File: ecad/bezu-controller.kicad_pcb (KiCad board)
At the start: 2 copper layers, 84 parts, among them Q1 40N06D, Q10 40N06D, Q11 40N06D, Q12 40N06D, Q13 40N06D, Q14 40N06D, Q15 40N06D, Q16 40N06D, Q17 40N06D, Q18 40N06D, Q19 40N06D, Q2 40N06D, Q20 40N06D, Q21 40N06D, Q22 40N06D, Q23 40N06D, Q24 40N06D, Q3 40N06D, Q4 40N06D, Q5 40N06D, Q6 40N06D, Q7 40N06D, Q8 40N06D, Q9 40N06D, U1 LM2105D, U10 LM2105D, U11 LM2105D, U12 LM2105D, U2 LM2105D, U3 LM2105D, U4 LM2105D, U5 LM2105D, U6 LM2105D, U7 LM2105D, U8 LM2105D, U9 LM2105D

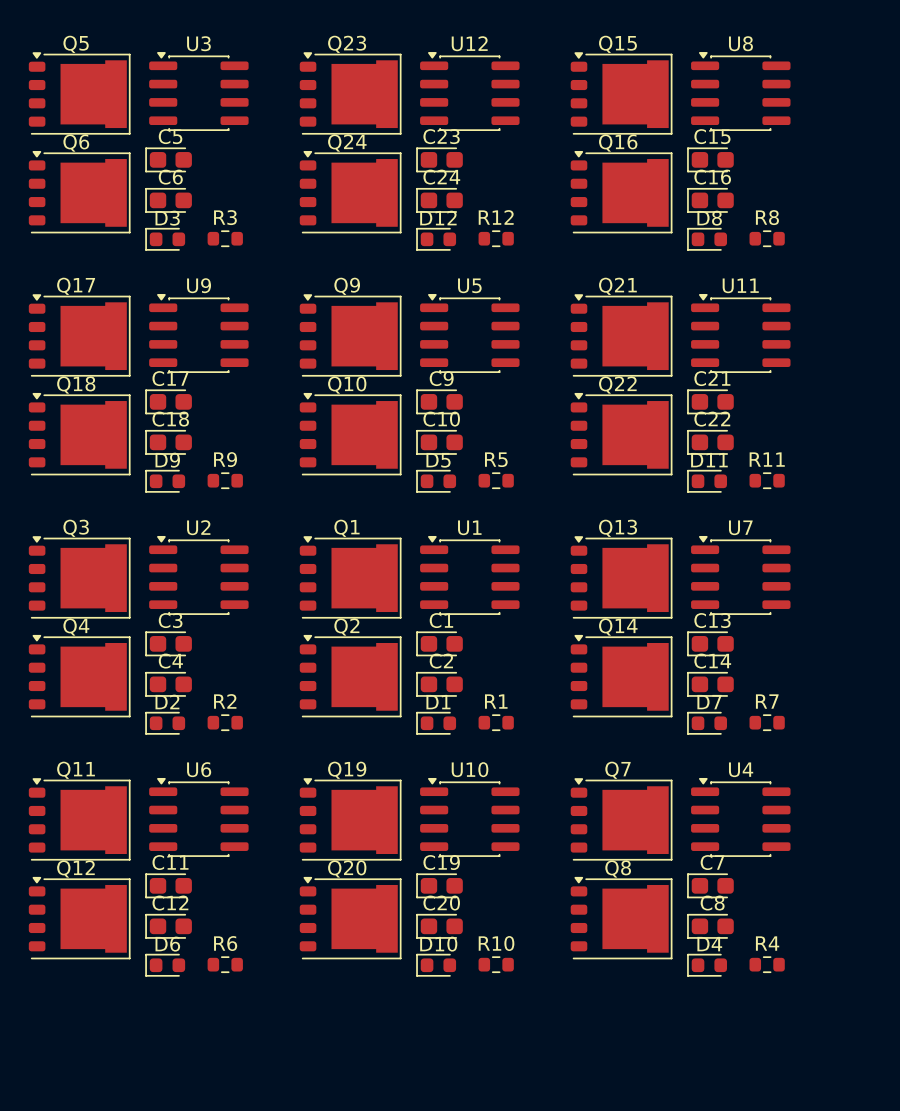
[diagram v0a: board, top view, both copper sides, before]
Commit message: Use IRS2104
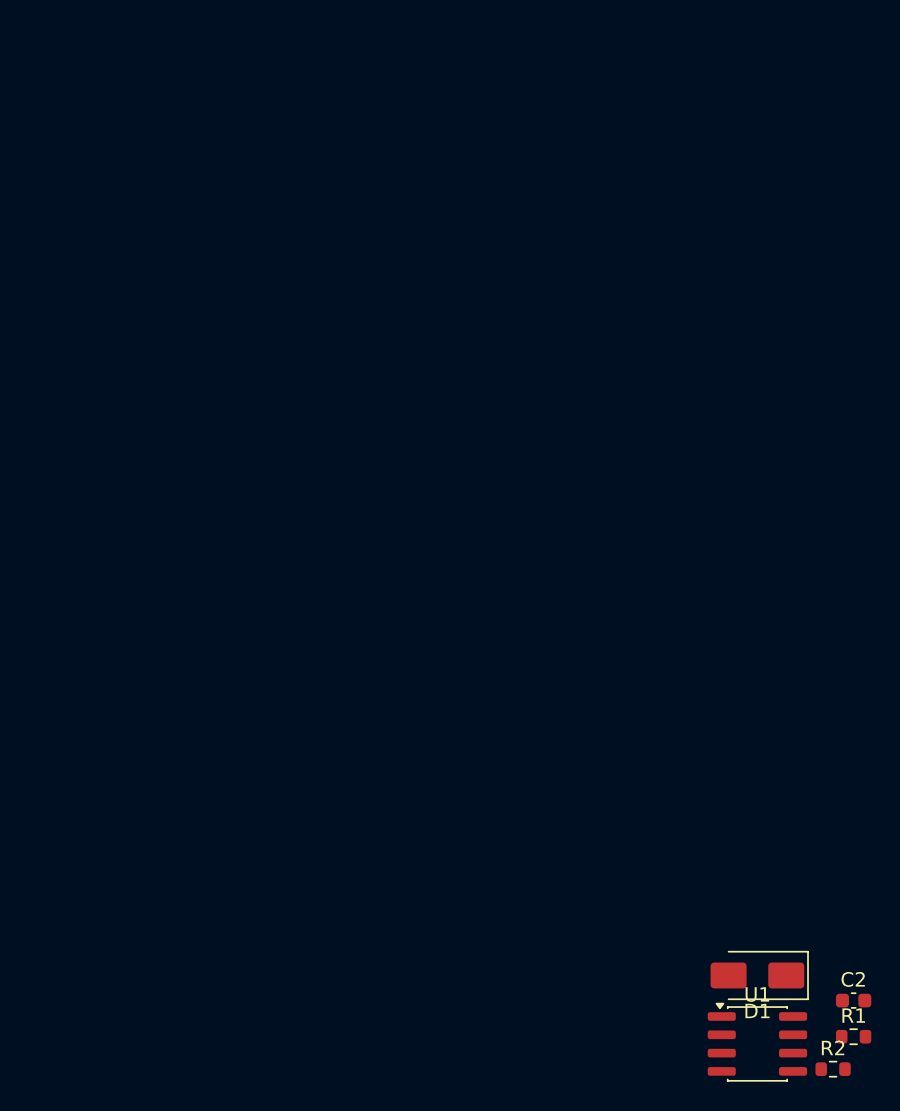
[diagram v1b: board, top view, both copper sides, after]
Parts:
- removed C1, C10, C11, C12, C13, C14, C15, C16, C17, C18, C19, C20, C21, C22, C23, C24, C3, C4, C5, C6, C7, C8, C9: C, Capacitor_Tantalum_SMD:CP_EIA-2012-12_Kemet-R
- removed D10, D11, D12, D2, D3, D4, D5, D6, D7, D8, D9: D, Diode_SMD:D_0603_1608Metric
- removed Q1, Q10, Q11, Q12, Q13, Q14, Q15, Q16, Q17, Q18, Q19, Q2, Q20, Q21, Q22, Q23, Q24, Q3, Q4, Q5, Q6, Q7, Q8, Q9: 40N06D, Package_DFN_QFN:PQFN-8-EP_6x5mm_P1.27mm_Generic
- removed R10, R11, R12, R3, R4, R5, R6, R7, R8, R9: R, Resistor_SMD:R_0603_1608Metric
- removed U10, U11, U12, U2, U3, U4, U5, U6, U7, U8, U9: LM2105D, Package_SO:SOIC-8_3.9x4.9mm_P1.27mm
- C2: footprint Capacitor_Tantalum_SMD:CP_EIA-2012-12_Kemet-R -> Capacitor_SMD:C_0603_1608Metric
- D1: value D -> ES1D; footprint Diode_SMD:D_0603_1608Metric -> Diode_SMD:D_SMA
- U1: value LM2105D -> IR2104
- moved R2 48.5 mm to (165.8, 123.2)
- moved U1 38.0 mm to (160.5, 121.5)
- moved C2 36.0 mm to (167.2, 118.5)
- moved R1 33.0 mm to (167.2, 121.0)
- moved D1 28.2 mm to (160.5, 116.8), turned to 180 degrees
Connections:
- C2 pad 1: unconnected-(C2-Pad1) -> Net-(D1-K)
- C2 pad 2: unconnected-(C2-Pad2) -> /H-Bridge/OUT
- D1 pad 1: (no net) -> Net-(D1-K)
- D1 pad 2: unconnected-(Q2-PadS) -> +12V
- R1 pad 1: unconnected-(Q2-PadS) -> Net-(U1-HO)
- R1 pad 2: (no net) -> Net-(Q1-PadG)
- R2 pad 1: Net-(D2-A) -> Net-(U1-LO)
- U1 pad 1: VDD -> +12V
- U1 pad 2: (no net) -> /H-Bridge/IN
- U1 pad 3: (no net) -> /H-Bridge/~{SD}
- U1 pad 5: (no net) -> Net-(U1-LO)
- U1 pad 6: unconnected-(C2-Pad2) -> /H-Bridge/OUT
- U1 pad 7: unconnected-(Q2-PadG) -> Net-(U1-HO)
- U1 pad 8: unconnected-(C2-Pad1) -> Net-(D1-K)

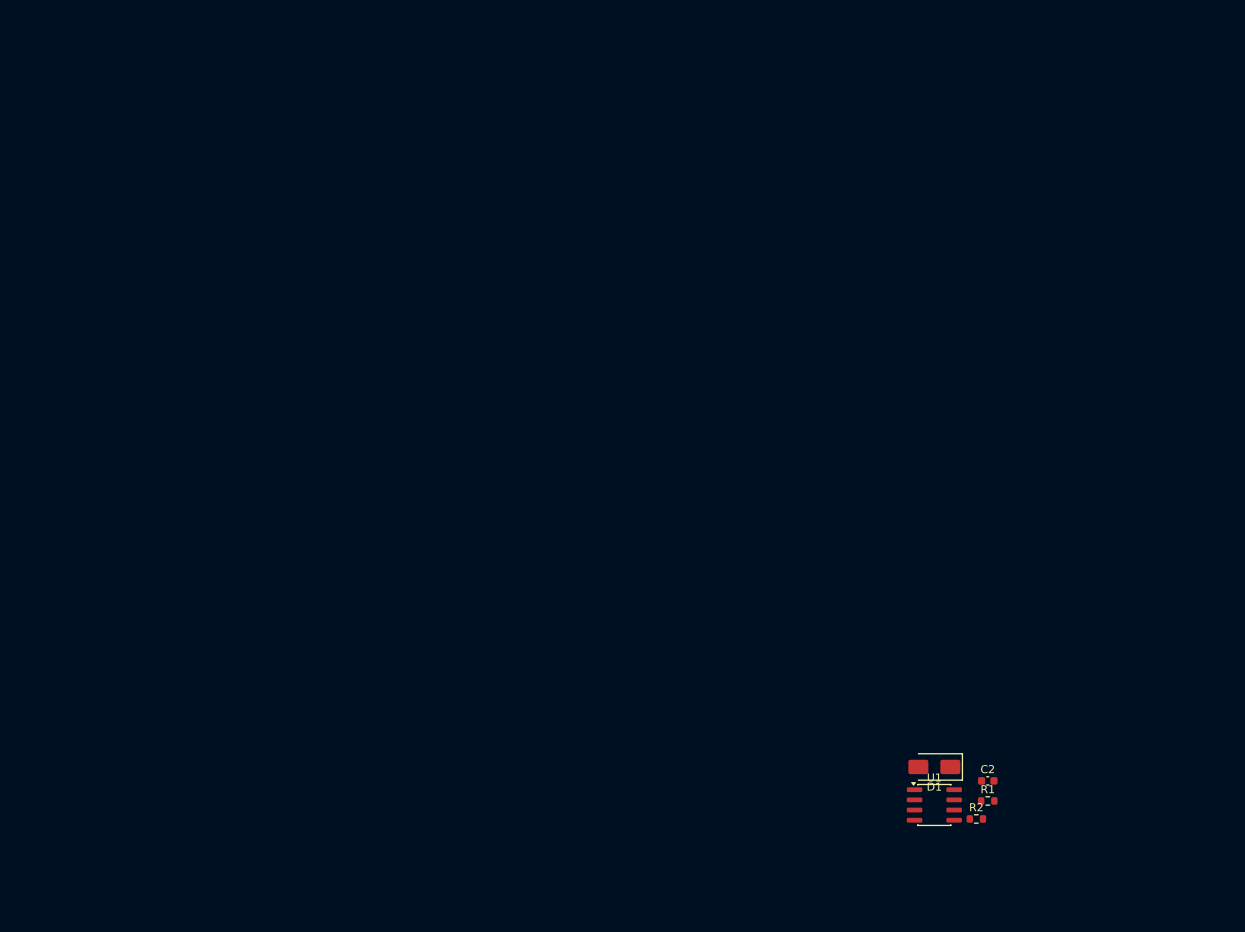
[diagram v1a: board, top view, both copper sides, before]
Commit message: Initial half bridge layout
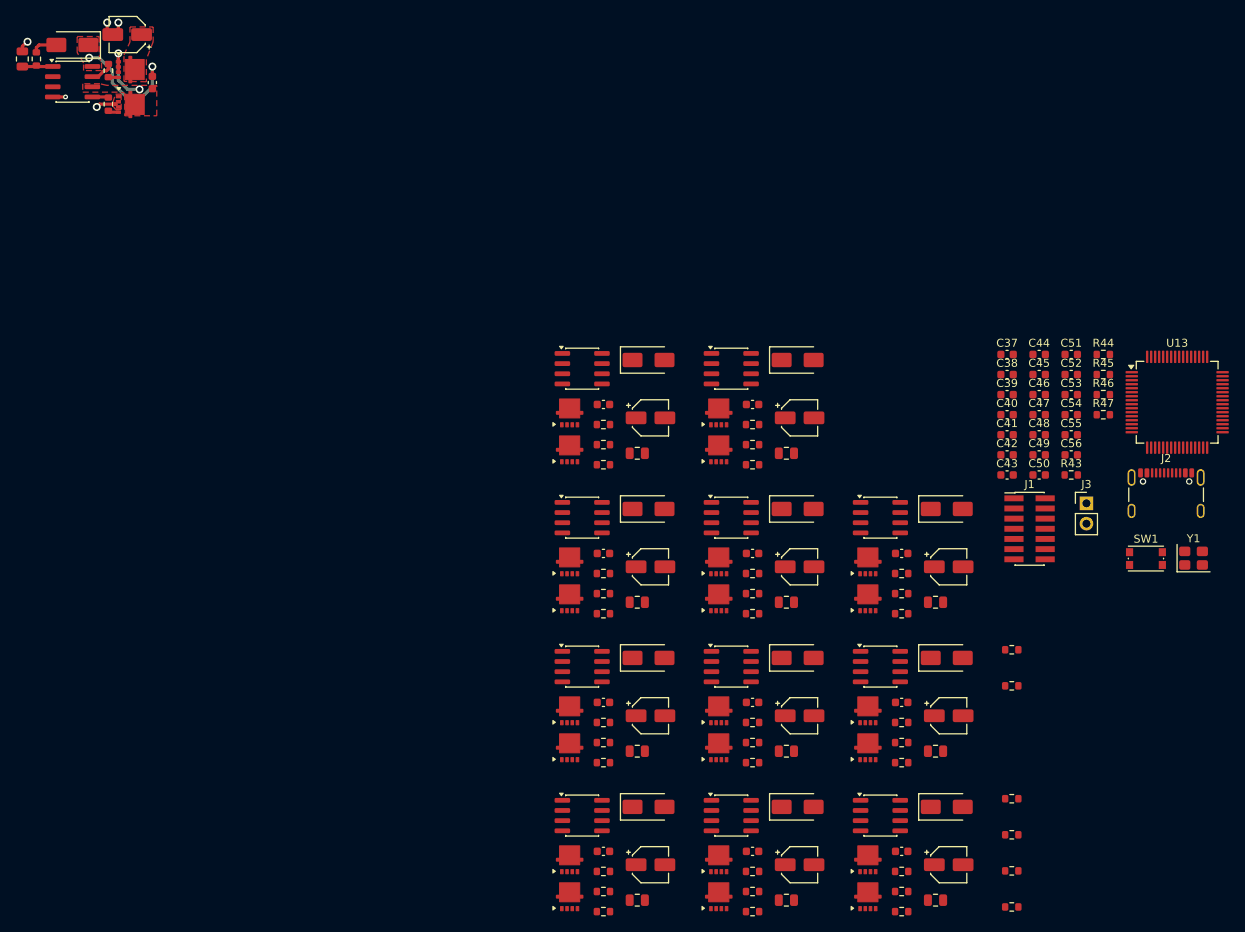
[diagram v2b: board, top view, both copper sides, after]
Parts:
- added C1: 470nF, Capacitor_SMD:C_0805_2012Metric, F.Cu at (46.5, 28.2)
- added C10: 470nF, Capacitor_SMD:C_0805_2012Metric, F.Cu at (123.4, 96.2)
- added C11: 47nF, Capacitor_SMD:C_0603_1608Metric, F.Cu at (119.1, 90.1)
- added C12: 4.7uF, Capacitor_SMD:CP_Elec_4x5.4, F.Cu at (125.0, 91.7)
- added C13: 470nF, Capacitor_SMD:C_0805_2012Metric, F.Cu at (123.4, 77.5)
- added C14: 47nF, Capacitor_SMD:C_0603_1608Metric, F.Cu at (119.1, 71.4)
- added C15: 4.7uF, Capacitor_SMD:CP_Elec_4x5.4, F.Cu at (125.0, 73.1)
- added C16: 470nF, Capacitor_SMD:C_0805_2012Metric, F.Cu at (160.6, 133.4)
- added C17: 47nF, Capacitor_SMD:C_0603_1608Metric, F.Cu at (156.4, 127.3)
- added C18: 4.7uF, Capacitor_SMD:CP_Elec_4x5.4, F.Cu at (162.3, 129.0)
- added C19: 470nF, Capacitor_SMD:C_0805_2012Metric, F.Cu at (160.6, 114.8)
- added C20: 47nF, Capacitor_SMD:C_0603_1608Metric, F.Cu at (156.4, 108.7)
- added C21: 4.7uF, Capacitor_SMD:CP_Elec_4x5.4, F.Cu at (162.3, 110.3)
- added C22: 470nF, Capacitor_SMD:C_0805_2012Metric, F.Cu at (142.0, 133.4)
- added C23: 47nF, Capacitor_SMD:C_0603_1608Metric, F.Cu at (137.8, 127.3)
- added C24: 4.7uF, Capacitor_SMD:CP_Elec_4x5.4, F.Cu at (143.7, 129.0)
- added C25: 470nF, Capacitor_SMD:C_0805_2012Metric, F.Cu at (142.0, 96.2)
- added C26: 47nF, Capacitor_SMD:C_0603_1608Metric, F.Cu at (137.8, 90.1)
- added C27: 4.7uF, Capacitor_SMD:CP_Elec_4x5.4, F.Cu at (143.7, 91.7)
- added C28: 470nF, Capacitor_SMD:C_0805_2012Metric, F.Cu at (123.4, 133.4)
- added C29: 47nF, Capacitor_SMD:C_0603_1608Metric, F.Cu at (119.1, 127.3)
- added C3: 4.7uF, Capacitor_SMD:CP_Elec_4x5.4, F.Cu at (59.6, 25.2)
- added C30: 4.7uF, Capacitor_SMD:CP_Elec_4x5.4, F.Cu at (125.0, 129.0)
- added C31: 470nF, Capacitor_SMD:C_0805_2012Metric, F.Cu at (142.0, 114.8)
- added C32: 47nF, Capacitor_SMD:C_0603_1608Metric, F.Cu at (137.8, 108.7)
- added C33: 4.7uF, Capacitor_SMD:CP_Elec_4x5.4, F.Cu at (143.7, 110.3)
- added C34: 470nF, Capacitor_SMD:C_0805_2012Metric, F.Cu at (160.6, 96.2)
- added C35: 47nF, Capacitor_SMD:C_0603_1608Metric, F.Cu at (156.4, 90.1)
- added C36: 4.7uF, Capacitor_SMD:CP_Elec_4x5.4, F.Cu at (162.3, 91.7)
- added C37: 4.7uF, Capacitor_SMD:C_0603_1608Metric, F.Cu at (169.6, 65.2)
- added C38: 2.2uF, Capacitor_SMD:C_0603_1608Metric, F.Cu at (169.6, 67.7)
- added C39: 2.2uF, Capacitor_SMD:C_0603_1608Metric, F.Cu at (169.6, 70.2)
- added C4: 470nF, Capacitor_SMD:C_0805_2012Metric, F.Cu at (142.0, 77.5)
- added C40: 100nF, Capacitor_SMD:C_0603_1608Metric, F.Cu at (169.6, 72.7)
- added C41: 100nF, Capacitor_SMD:C_0603_1608Metric, F.Cu at (169.6, 75.2)
- added C42: 100nF, Capacitor_SMD:C_0603_1608Metric, F.Cu at (169.6, 77.7)
- added C43: 100nF, Capacitor_SMD:C_0603_1608Metric, F.Cu at (169.6, 80.2)
- added C44: 100nF, Capacitor_SMD:C_0603_1608Metric, F.Cu at (173.6, 65.2)
- added C45: 100nF, Capacitor_SMD:C_0603_1608Metric, F.Cu at (173.6, 67.7)
- added C46: 100nF, Capacitor_SMD:C_0603_1608Metric, F.Cu at (173.6, 70.2)
- added C47: 100nF, Capacitor_SMD:C_0603_1608Metric, F.Cu at (173.6, 72.7)
- added C48: 100nF, Capacitor_SMD:C_0603_1608Metric, F.Cu at (173.6, 75.2)
- added C49: 100nF, Capacitor_SMD:C_0603_1608Metric, F.Cu at (173.6, 77.7)
- added C5: 47nF, Capacitor_SMD:C_0603_1608Metric, F.Cu at (137.8, 71.4)
- added C50: 100nF, Capacitor_SMD:C_0603_1608Metric, F.Cu at (173.6, 80.2)
- added C51: 100nF, Capacitor_SMD:C_0603_1608Metric, F.Cu at (177.6, 65.2)
- added C52: 100nF, Capacitor_SMD:C_0603_1608Metric, F.Cu at (177.6, 67.7)
- added C53: 100nF, Capacitor_SMD:C_0603_1608Metric, F.Cu at (177.6, 70.2)
- added C54: 100nF, Capacitor_SMD:C_0603_1608Metric, F.Cu at (177.6, 72.7)
- added C55: 16pF, Capacitor_SMD:C_0603_1608Metric, F.Cu at (177.6, 75.2)
- added C56: 16pF, Capacitor_SMD:C_0603_1608Metric, F.Cu at (177.6, 77.7)
- added C6: 4.7uF, Capacitor_SMD:CP_Elec_4x5.4, F.Cu at (143.7, 73.1)
- added C7: 470nF, Capacitor_SMD:C_0805_2012Metric, F.Cu at (123.4, 114.8)
- added C8: 47nF, Capacitor_SMD:C_0603_1608Metric, F.Cu at (119.1, 108.7)
- added C9: 4.7uF, Capacitor_SMD:CP_Elec_4x5.4, F.Cu at (125.0, 110.3)
- added D10: ES1D, Diode_SMD:D_SMA, F.Cu at (124.8, 121.7)
- added D11: ES1D, Diode_SMD:D_SMA, F.Cu at (143.4, 103.1)
- added D12: ES1D, Diode_SMD:D_SMA, F.Cu at (162.1, 84.5)
- added D2: ES1D, Diode_SMD:D_SMA, F.Cu at (143.4, 65.9)
- added D3: ES1D, Diode_SMD:D_SMA, F.Cu at (124.8, 103.1)
- added D4: ES1D, Diode_SMD:D_SMA, F.Cu at (124.8, 84.5)
- added D5: ES1D, Diode_SMD:D_SMA, F.Cu at (124.8, 65.9)
- added D6: ES1D, Diode_SMD:D_SMA, F.Cu at (162.1, 121.7)
- added D7: ES1D, Diode_SMD:D_SMA, F.Cu at (162.1, 103.1)
- added D8: ES1D, Diode_SMD:D_SMA, F.Cu at (143.4, 121.7)
- added D9: ES1D, Diode_SMD:D_SMA, F.Cu at (143.4, 84.5)
- added J1: ST_STDC14, Connector_PinHeader_1.27mm:PinHeader_2x07_P1.27mm_Vertical_SMD, F.Cu at (172.4, 87.0)
- added J2: GCT 4105, Connector_USB:USB_C_Receptacle_GCT_USB4105-xx-A_16P_TopMnt_Horizontal, F.Cu at (189.5, 83.7)
- added J3: Conn_01x02, Connector_PinHeader_2.54mm:PinHeader_1x02_P2.54mm_Vertical, F.Cu at (179.5, 83.8)
- added Q1: 40N06D, bezu-controller:PDFN3x3, F.Cu at (60.0, 29.6)
- added Q10: 40N06D, bezu-controller:PDFN3x3, F.Cu at (114.9, 77.1)
- added Q11: 40N06D, bezu-controller:PDFN3x3, F.Cu at (152.2, 128.3)
- added Q12: 40N06D, bezu-controller:PDFN3x3, F.Cu at (152.2, 133.0)
- added Q13: 40N06D, bezu-controller:PDFN3x3, F.Cu at (152.2, 109.7)
- added Q14: 40N06D, bezu-controller:PDFN3x3, F.Cu at (152.2, 114.3)
- added Q15: 40N06D, bezu-controller:PDFN3x3, F.Cu at (133.6, 128.3)
- added Q16: 40N06D, bezu-controller:PDFN3x3, F.Cu at (133.6, 133.0)
- added Q17: 40N06D, bezu-controller:PDFN3x3, F.Cu at (133.6, 91.1)
- added Q18: 40N06D, bezu-controller:PDFN3x3, F.Cu at (133.6, 95.7)
- added Q19: 40N06D, bezu-controller:PDFN3x3, F.Cu at (114.9, 128.3)
- added Q2: 40N06D, bezu-controller:PDFN3x3, F.Cu at (60.0, 33.9)
- added Q20: 40N06D, bezu-controller:PDFN3x3, F.Cu at (114.9, 133.0)
- added Q21: 40N06D, bezu-controller:PDFN3x3, F.Cu at (133.6, 109.7)
- added Q22: 40N06D, bezu-controller:PDFN3x3, F.Cu at (133.6, 114.3)
- added Q23: 40N06D, bezu-controller:PDFN3x3, F.Cu at (152.2, 91.1)
- added Q24: 40N06D, bezu-controller:PDFN3x3, F.Cu at (152.2, 95.7)
- added Q3: 40N06D, bezu-controller:PDFN3x3, F.Cu at (133.6, 72.5)
- added Q4: 40N06D, bezu-controller:PDFN3x3, F.Cu at (133.6, 77.1)
- added Q5: 40N06D, bezu-controller:PDFN3x3, F.Cu at (114.9, 109.7)
- added Q6: 40N06D, bezu-controller:PDFN3x3, F.Cu at (114.9, 114.3)
- added Q7: 40N06D, bezu-controller:PDFN3x3, F.Cu at (114.9, 91.1)
- added Q8: 40N06D, bezu-controller:PDFN3x3, F.Cu at (114.9, 95.7)
- added Q9: 40N06D, bezu-controller:PDFN3x3, F.Cu at (114.9, 72.5)
- added R10: 10R, Resistor_SMD:R_0603_1608Metric, F.Cu at (119.1, 113.7)
- added R11: 10R, Resistor_SMD:R_0603_1608Metric, F.Cu at (119.1, 116.2)
- added R12: 2.2R, Resistor_SMD:R_0603_1608Metric, F.Cu at (119.1, 92.6)
- added R13: 10R, Resistor_SMD:R_0603_1608Metric, F.Cu at (119.1, 95.1)
- added R14: 10R, Resistor_SMD:R_0603_1608Metric, F.Cu at (119.1, 97.6)
- added R15: 10K, Resistor_SMD:R_0603_1608Metric, F.Cu at (170.2, 106.6)
- added R16: 2.2R, Resistor_SMD:R_0603_1608Metric, F.Cu at (119.1, 74.0)
- added R17: 10R, Resistor_SMD:R_0603_1608Metric, F.Cu at (119.1, 76.5)
- added R18: 10R, Resistor_SMD:R_0603_1608Metric, F.Cu at (119.1, 79.0)
- added R19: 2.2R, Resistor_SMD:R_0603_1608Metric, F.Cu at (156.4, 129.8)
- added R20: 10R, Resistor_SMD:R_0603_1608Metric, F.Cu at (156.4, 132.3)
- added R21: 10R, Resistor_SMD:R_0603_1608Metric, F.Cu at (156.4, 134.8)
- added R22: 10K, Resistor_SMD:R_0603_1608Metric, F.Cu at (170.2, 134.2)
- added R23: 2.2R, Resistor_SMD:R_0603_1608Metric, F.Cu at (156.4, 111.2)
- added R24: 10R, Resistor_SMD:R_0603_1608Metric, F.Cu at (156.4, 113.7)
- added R25: 10R, Resistor_SMD:R_0603_1608Metric, F.Cu at (156.4, 116.2)
- added R26: 2.2R, Resistor_SMD:R_0603_1608Metric, F.Cu at (137.8, 129.8)
- added R27: 10R, Resistor_SMD:R_0603_1608Metric, F.Cu at (137.8, 132.3)
- added R28: 10R, Resistor_SMD:R_0603_1608Metric, F.Cu at (137.8, 134.8)
- added R29: 10K, Resistor_SMD:R_0603_1608Metric, F.Cu at (170.2, 120.7)
- added R3: 10R, Resistor_SMD:R_0603_1608Metric, F.Cu at (57.2, 29.7)
- added R30: 2.2R, Resistor_SMD:R_0603_1608Metric, F.Cu at (137.8, 92.6)
- added R31: 10R, Resistor_SMD:R_0603_1608Metric, F.Cu at (137.8, 95.1)
- added R32: 10R, Resistor_SMD:R_0603_1608Metric, F.Cu at (137.8, 97.6)
- added R33: 2.2R, Resistor_SMD:R_0603_1608Metric, F.Cu at (119.1, 129.8)
- added R34: 10R, Resistor_SMD:R_0603_1608Metric, F.Cu at (119.1, 132.3)
- added R35: 10R, Resistor_SMD:R_0603_1608Metric, F.Cu at (119.1, 134.8)
- added R36: 10K, Resistor_SMD:R_0603_1608Metric, F.Cu at (170.2, 125.2)
- added R37: 2.2R, Resistor_SMD:R_0603_1608Metric, F.Cu at (137.8, 111.2)
- added R38: 10R, Resistor_SMD:R_0603_1608Metric, F.Cu at (137.8, 113.7)
- added R39: 10R, Resistor_SMD:R_0603_1608Metric, F.Cu at (137.8, 116.2)
- added R4: 10R, Resistor_SMD:R_0603_1608Metric, F.Cu at (57.2, 33.9)
- added R40: 2.2R, Resistor_SMD:R_0603_1608Metric, F.Cu at (156.4, 92.6)
- added R41: 10R, Resistor_SMD:R_0603_1608Metric, F.Cu at (156.4, 95.1)
- added R42: 10R, Resistor_SMD:R_0603_1608Metric, F.Cu at (156.4, 97.6)
- added R43: 10K, Resistor_SMD:R_0603_1608Metric, F.Cu at (177.6, 80.2)
- added R44: 100R, Resistor_SMD:R_0603_1608Metric, F.Cu at (181.6, 65.2)
- added R45: 5k1, Resistor_SMD:R_0603_1608Metric, F.Cu at (181.6, 67.7)
- added R46: 5k1, Resistor_SMD:R_0603_1608Metric, F.Cu at (181.6, 70.2)
- added R47: 10K, Resistor_SMD:R_0603_1608Metric, F.Cu at (181.6, 72.7)
- added R5: 2.2R, Resistor_SMD:R_0603_1608Metric, F.Cu at (137.8, 74.0)
- added R6: 10R, Resistor_SMD:R_0603_1608Metric, F.Cu at (137.8, 76.5)
- added R7: 10R, Resistor_SMD:R_0603_1608Metric, F.Cu at (137.8, 79.0)
- added R8: 10K, Resistor_SMD:R_0603_1608Metric, F.Cu at (170.2, 129.7)
- added R9: 2.2R, Resistor_SMD:R_0603_1608Metric, F.Cu at (119.1, 111.2)
- added SW1: SW_Push, Button_Switch_SMD:SW_Push_1P1T_NO_CK_KMR2, F.Cu at (186.9, 90.7)
- added U10: IR2104, Package_SO:SOIC-8_3.9x4.9mm_P1.27mm, F.Cu at (116.5, 122.8)
- added U11: IR2104, Package_SO:SOIC-8_3.9x4.9mm_P1.27mm, F.Cu at (135.1, 104.2)
- added U12: IR2104, Package_SO:SOIC-8_3.9x4.9mm_P1.27mm, F.Cu at (153.8, 85.6)
- added U13: STM32F405RGTx, Package_QFP:LQFP-64_10x10mm_P0.5mm, F.Cu at (190.8, 71.2)
- added U2: IR2104, Package_SO:SOIC-8_3.9x4.9mm_P1.27mm, F.Cu at (135.1, 67.0)
- added U3: IR2104, Package_SO:SOIC-8_3.9x4.9mm_P1.27mm, F.Cu at (116.5, 104.2)
- added U4: IR2104, Package_SO:SOIC-8_3.9x4.9mm_P1.27mm, F.Cu at (116.5, 85.6)
- added U5: IR2104, Package_SO:SOIC-8_3.9x4.9mm_P1.27mm, F.Cu at (116.5, 67.0)
- added U6: IR2104, Package_SO:SOIC-8_3.9x4.9mm_P1.27mm, F.Cu at (153.8, 122.8)
- added U7: IR2104, Package_SO:SOIC-8_3.9x4.9mm_P1.27mm, F.Cu at (153.8, 104.2)
- added U8: IR2104, Package_SO:SOIC-8_3.9x4.9mm_P1.27mm, F.Cu at (135.1, 122.8)
- added U9: IR2104, Package_SO:SOIC-8_3.9x4.9mm_P1.27mm, F.Cu at (135.1, 85.6)
- added Y1: 12MHz, Crystal:Crystal_SMD_3225-4Pin_3.2x2.5mm, F.Cu at (192.9, 90.7)
- C2: value C -> 47nF
- R1: value R -> 10K
- R2: value R -> 2.2R
- moved R2 151.1 mm to (48.2, 28.2), turned to 90 degrees
- moved U1 140.6 mm to (52.8, 31.1)
- moved D1 140.6 mm to (52.8, 26.5)
- moved C2 136.1 mm to (62.8, 31.2), turned to -90 degrees
- moved R1 19.1 mm to (170.2, 102.1)
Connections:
- net /H-Bridge/IN renamed /-PITCH H-Bridge/IN1
- net /H-Bridge/OUT renamed /-PITCH H-Bridge/OUT1
- D1 pad 2: +12V -> Net-(D1-A)
- R1 pad 1: Net-(U1-HO) -> /-PITCH H-Bridge/~{SD}
- R1 pad 2: Net-(Q1-PadG) -> GND
- R2 pad 1: Net-(U1-LO) -> +12V
- R2 pad 2: Net-(Q2-PadG) -> Net-(D1-A)
- U1 pad 3: /H-Bridge/~{SD} -> /-PITCH H-Bridge/~{SD}
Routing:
- net Net-(D1-K): track 0.00 -> 15.0 mm, vias 0 -> 2
- net GND: track 0.00 -> 9.59 mm, vias 0 -> 5
- net /-PITCH H-Bridge/OUT1: track 0.00 -> 8.83 mm, vias 0 -> 2
- net +12V: track 0.00 -> 3.80 mm
- net Net-(D1-A): track 0.00 -> 3.22 mm
- net Net-(U1-HO): track 0.00 -> 3.02 mm
- net Net-(U1-LO): track 0.00 -> 2.03 mm
- net Net-(Q2-PadG): track 0.00 -> 1.33 mm
- net Net-(Q1-PadG): track 0.00 -> 1.26 mm
- added copper zone on F.Cu, net /-PITCH H-Bridge/OUT1
- added copper zone on F.Cu, net GND
- added copper zone on F.Cu, net Net-(D1-K)
- added copper zone on F.Cu, net Vdrive
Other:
- copper layers 2 -> 4

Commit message: More work on layout
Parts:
- removed C15, C21, C27, C3, C33, C9: 4.7uF, Capacitor_SMD:CP_Elec_4x5.4
- moved C1 106.8 mm to (135.7, 86.9)
- moved D1 106.8 mm to (141.9, 85.2)
- moved Q2 106.8 mm to (149.2, 92.6)
- moved R2 106.8 mm to (137.4, 86.9)
- moved R4 106.8 mm to (146.4, 92.6)
- moved U1 106.8 mm to (142.0, 89.8)
- moved C2 106.8 mm to (151.9, 89.9)
- moved Q1 106.8 mm to (149.2, 88.3)
- moved R3 106.8 mm to (146.4, 88.4)
- moved J2 87.8 mm to (102.1, 91.8), turned to -90 degrees
- moved Q9 79.9 mm to (193.2, 88.3), turned to -90 degrees
- moved Q10 79.8 mm to (193.2, 92.6), turned to -90 degrees
- moved C14 79.0 mm to (195.9, 89.9), turned to -90 degrees
- moved U13 77.7 mm to (115.5, 90.3), turned to 180 degrees
- moved C54 74.5 mm to (108.4, 100.2)
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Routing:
- net GND: track 9.59 -> 93.6 mm, vias 5 -> 48
- net +12V: track 3.80 -> 45.6 mm
- net Net-(D9-K): track 0.00 -> 15.0 mm, vias 0 -> 2
- net Net-(D7-K): track 0.00 -> 15.0 mm, vias 0 -> 2
- net Net-(D3-K): track 0.00 -> 15.0 mm, vias 0 -> 2
- net Net-(D11-K): track 0.00 -> 15.0 mm, vias 0 -> 2
- net Net-(D5-K): track 0.00 -> 15.0 mm, vias 0 -> 2
- net Net-(D8-K): track 0.00 -> 15.0 mm, vias 0 -> 2
- net Net-(D6-K): track 0.00 -> 15.0 mm, vias 0 -> 2
- net Net-(D4-K): track 0.00 -> 15.0 mm, vias 0 -> 2
- net Net-(D2-K): track 0.00 -> 15.0 mm, vias 0 -> 2
- net Net-(D12-K): track 0.00 -> 15.0 mm, vias 0 -> 2
- net Net-(D10-K): track 0.00 -> 15.0 mm, vias 0 -> 2
- net /YAW H-Bridge3/OUT2: track 0.00 -> 8.83 mm, vias 0 -> 2
- net /-YAW H-Bridge2/OUT2: track 0.00 -> 8.83 mm, vias 0 -> 2
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- added copper zone on F.Cu, net /-PITCH H-Bridge/OUT2
- added copper zone on F.Cu, net /-ROLL H-Bridge1/OUT1
- added copper zone on F.Cu, net /-ROLL H-Bridge1/OUT2
- added copper zone on F.Cu, net /-YAW H-Bridge2/OUT1
- added copper zone on F.Cu, net /-YAW H-Bridge2/OUT2
- added copper zone on F.Cu, net /PITCH H-Bridge1/OUT1
- added copper zone on F.Cu, net /PITCH H-Bridge1/OUT2
- added copper zone on F.Cu, net /ROLL H-Bridge2/OUT1
- added copper zone on F.Cu, net /ROLL H-Bridge2/OUT2
- added copper zone on F.Cu, net /YAW H-Bridge3/OUT1
- added copper zone on F.Cu, net /YAW H-Bridge3/OUT2
- added copper zone on F.Cu, net Net-(D10-K)
- added copper zone on F.Cu, net Net-(D11-K)
- added copper zone on F.Cu, net Net-(D12-K)
- added copper zone on F.Cu, net Net-(D2-K)
- added copper zone on F.Cu, net Net-(D3-K)
- added copper zone on F.Cu, net Net-(D4-K)
- added copper zone on F.Cu, net Net-(D5-K)
- added copper zone on F.Cu, net Net-(D6-K)
- added copper zone on F.Cu, net Net-(D7-K)
- added copper zone on F.Cu, net Net-(D8-K)
- added copper zone on F.Cu, net Net-(D9-K)
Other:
- board outline added: 99 x 48.3 mm
